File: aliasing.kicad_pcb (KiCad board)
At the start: 2 copper layers, 50 x 57 mm, 16 parts, among them J1001 Conn_Coaxial, J1002 Conn_Coaxial, J1003 Conn_Coaxial, J1004 Conn_Coaxial, J1005 Conn_Coaxial, J1006 Conn_Coaxial, J1007 Conn_01x01_Female, J1008 Conn_01x01_Female, J1009 Conn_01x01_Female, J1010 Conn_01x01_Female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

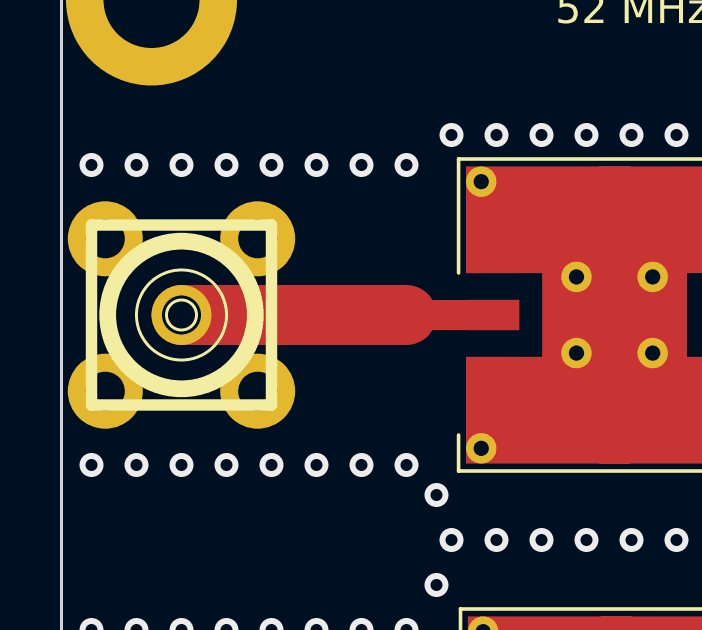
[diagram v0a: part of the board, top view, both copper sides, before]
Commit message: Silkmask cleaning, new set of Gerber files
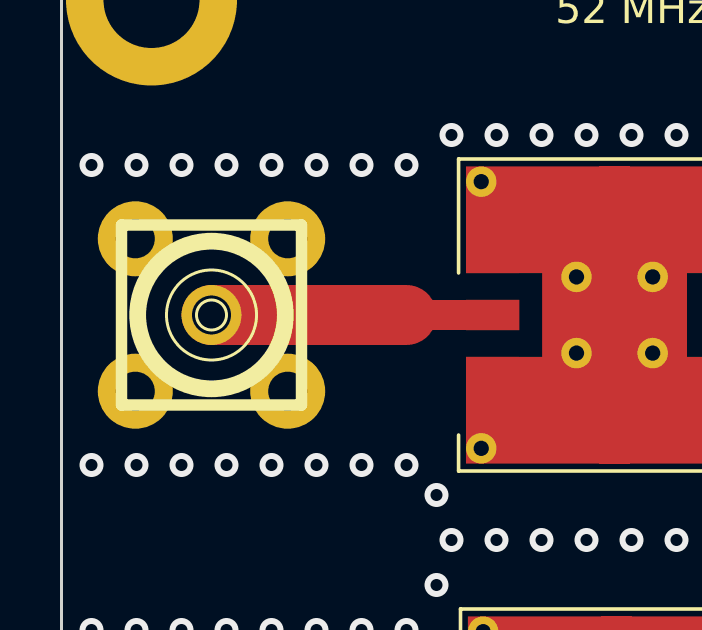
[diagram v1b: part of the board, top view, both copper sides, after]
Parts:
- added REF**: KiCad-Logo2_6mm_SilkScreen, Symbol:KiCad-Logo2_6mm_SilkScreen, B.Cu at (148.5, 44.5)
- added REF**: OSHW-Logo2_7.3x6mm_SilkScreen, Symbol:OSHW-Logo2_7.3x6mm_SilkScreen, B.Cu at (173.0, 72.0)
- moved J1002 1.00 mm to (140.0, 50.0)
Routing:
- net Net-(J1002-Pad1): track 10.4 -> 9.37 mm

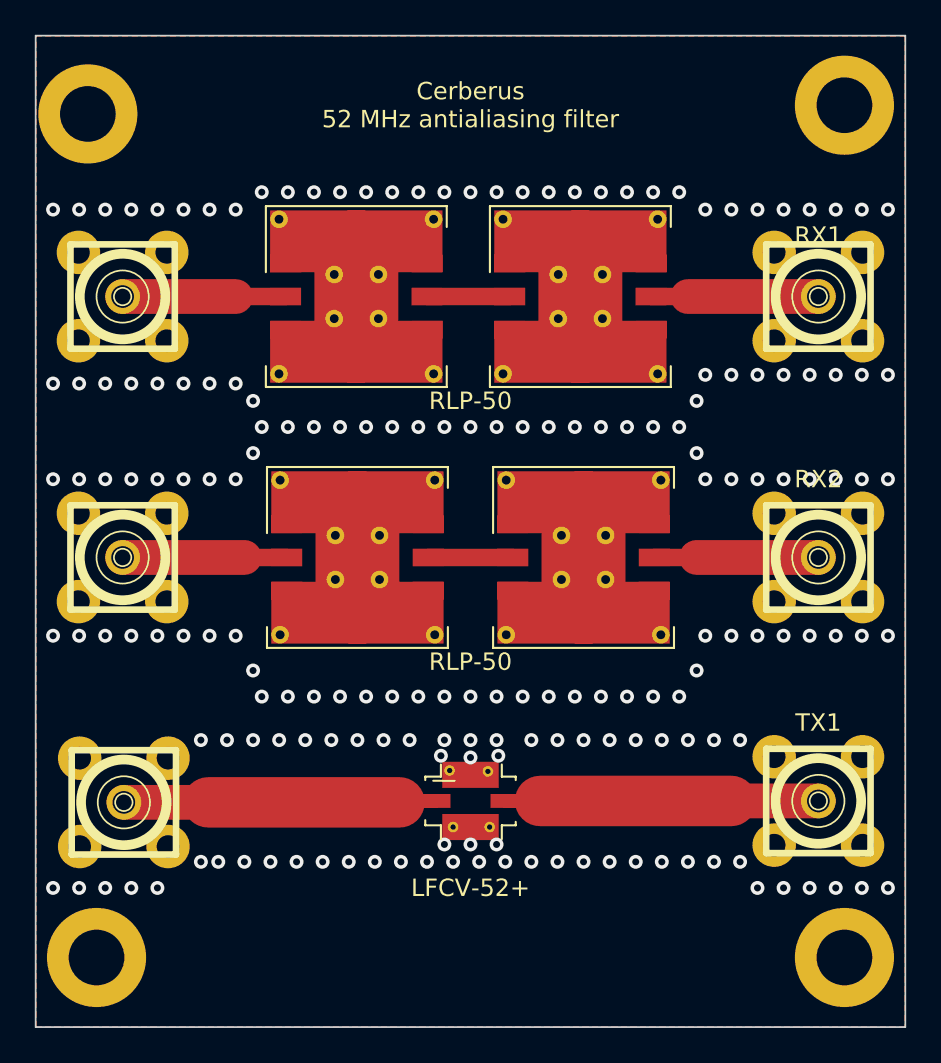
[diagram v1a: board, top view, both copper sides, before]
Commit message: excentred mounting hole corrected
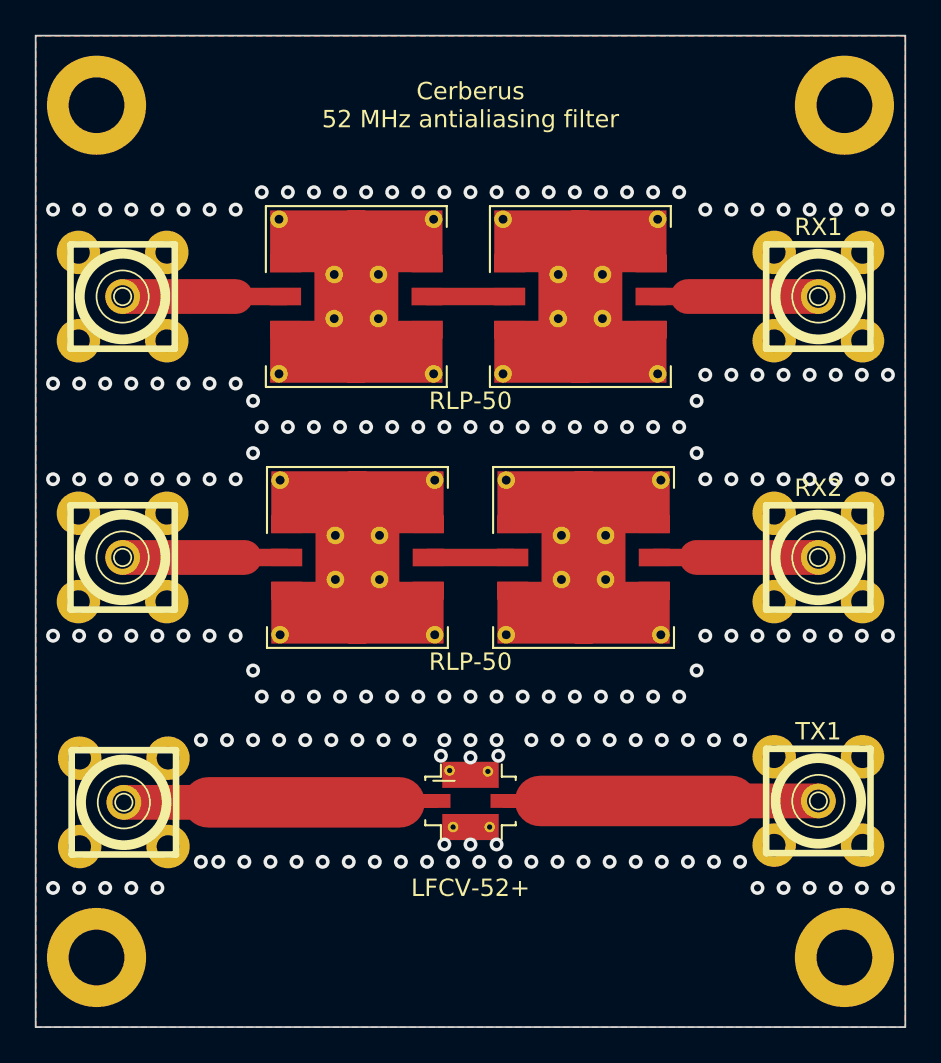
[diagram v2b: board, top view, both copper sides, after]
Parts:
- moved J1010 0.71 mm to (138.5, 39.0)
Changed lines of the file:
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@@
   )
   (footprint "MountingHole:MountingHole_3.2mm_M3_ISO7380_Pad" (layer "F.Cu")
-    (at 138 39.5)
+    (at 138.5 39)
     (descr "Mounting Hole 3.2mm, M3, ISO7380")
     (tags "mounting hole 3.2mm m3 iso7380")
@@
     (effects (font (size 1 1) (thickness 0.15) italic) (justify mirror))
   )
-  (gr_text "TX1\n" (at 180 74.5) (layer "F.SilkS")
+  (gr_text "TX1\n" (at 180 75) (layer "F.SilkS")
     (effects (font (size 1 1) (thickness 0.15)))
   )
@@
     (effects (font (size 1 1) (thickness 0.15)))
   )
-  (gr_text "RX1\n" (at 180 46.5) (layer "F.SilkS")
+  (gr_text "RX1\n" (at 180 46) (layer "F.SilkS")
     (effects (font (size 1 1) (thickness 0.15)))
   )
@@
     (effects (font (size 1 1) (thickness 0.15)))
   )
-  (gr_text "RX2\n" (at 180 60.5) (layer "F.SilkS")
+  (gr_text "RX2\n" (at 180 61) (layer "F.SilkS")
     (effects (font (size 1 1) (thickness 0.15)))
   )
